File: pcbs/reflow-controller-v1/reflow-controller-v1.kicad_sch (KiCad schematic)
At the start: 19 parts, among them J1 PinHeader 1x03 P2.54mm, J101 EB163A-03-C-180, J102 EB163A-02-C-180, J103 EB163A-02-C-180, J104 EB163A-02-C-180, J105 EB163A-02-C-180, J106 PinHeader 1x03 P2.54mm, M101 47053-1000

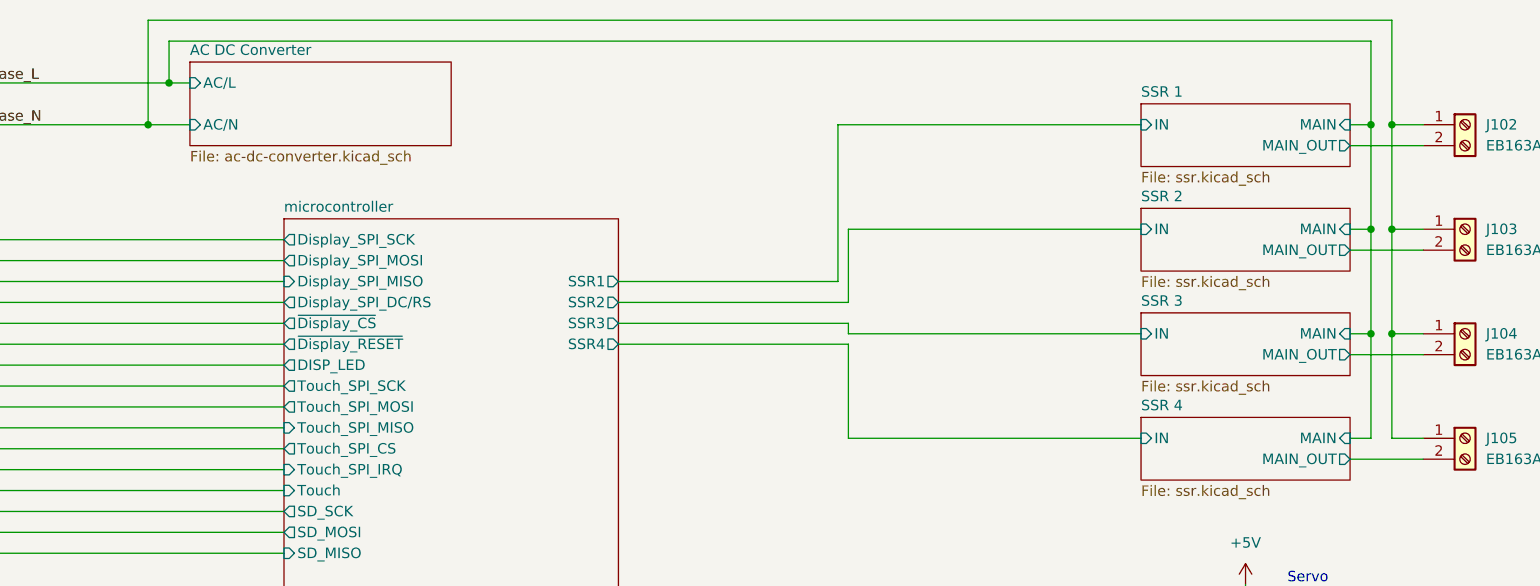
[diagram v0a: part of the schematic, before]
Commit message: add zero crossing detector
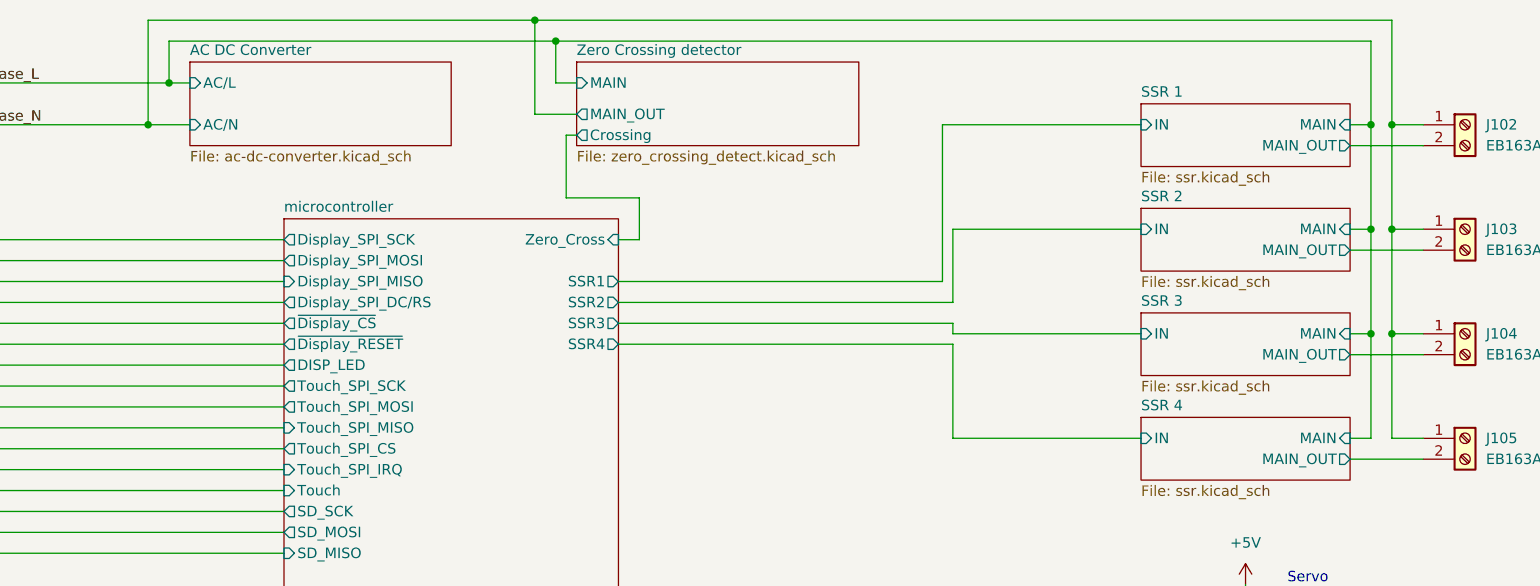
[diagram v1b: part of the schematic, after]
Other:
- added sheet Zero Crossing detector (zero_crossing_detect.kicad_sch)
- sheet microcontroller ports: added Zero_Cross; removed none
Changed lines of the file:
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@@
 	)
 	(junction
+		(at 132.08 13.97)
+		(diameter 0)
+		(color 0 0 0 0)
+	)
+	(junction
 		(at 233.68 39.37)
 		(diameter 0)
@@
 		(color 0 0 0 0)
 	)
+	(junction
+		(at 134.62 16.51)
+		(diameter 0)
+		(color 0 0 0 0)
+	)
 	(no_connect
 		(at 240.03 139.7)
@@
 	(wire
 		(pts
+			(xy 134.62 16.51) (xy 233.68 16.51)
+		)
+		(stroke
+			(width 0)
+			(type default)
+		)
+	)
+	(wire
+		(pts
 			(xy 133.35 167.64) (xy 133.35 177.8)
 		)
@@
 	(wire
 		(pts
+			(xy 144.78 40.64) (xy 142.24 40.64)
+		)
+		(stroke
+			(width 0)
+			(type default)
+		)
+	)
+	(wire
+		(pts
 			(xy 185.42 121.92) (xy 185.42 132.08)
 		)
@@
 	(wire
 		(pts
-			(xy 142.24 50.8) (xy 170.18 50.8)
+			(xy 142.24 50.8) (xy 182.88 50.8)
 		)
 		(stroke
@@
 	(wire
 		(pts
-			(xy 170.18 52.07) (xy 205.74 52.07)
+			(xy 182.88 52.07) (xy 205.74 52.07)
 		)
 		(stroke
@@
 	(wire
 		(pts
-			(xy 205.74 64.77) (xy 170.18 64.77)
+			(xy 205.74 64.77) (xy 182.88 64.77)
 		)
 		(stroke
@@
 	(wire
 		(pts
+			(xy 137.16 21.59) (xy 134.62 21.59)
+		)
+		(stroke
+			(width 0)
+			(type default)
+		)
+	)
+	(wire
+		(pts
 			(xy 54.61 144.78) (xy 101.6 144.78)
 		)
@@
 	(wire
 		(pts
-			(xy 168.91 45.72) (xy 168.91 26.67)
+			(xy 181.61 45.72) (xy 181.61 26.67)
 		)
 		(stroke
@@
 	(wire
 		(pts
-			(xy 142.24 48.26) (xy 170.18 48.26)
+			(xy 142.24 48.26) (xy 182.88 48.26)
+		)
+		(stroke
+			(width 0)
+			(type default)
+		)
+	)
+	(wire
+		(pts
+			(xy 135.89 35.56) (xy 144.78 35.56)
 		)
 		(stroke
@@
 	(wire
 		(pts
+			(xy 137.16 25.4) (xy 132.08 25.4)
+		)
+		(stroke
+			(width 0)
+			(type default)
+		)
+	)
+	(wire
+		(pts
 			(xy 49.53 63.5) (xy 101.6 63.5)
 		)
@@
 	(wire
 		(pts
+			(xy 137.16 27.94) (xy 135.89 27.94)
+		)
+		(stroke
+			(width 0)
+			(type default)
+		)
+	)
+	(wire
+		(pts
 			(xy 49.53 71.12) (xy 101.6 71.12)
 		)
@@
 	(wire
 		(pts
-			(xy 236.22 13.97) (xy 85.09 13.97)
+			(xy 144.78 35.56) (xy 144.78 40.64)
+		)
+		(stroke
+			(width 0)
+			(type default)
+		)
+	)
+	(wire
+		(pts
+			(xy 236.22 13.97) (xy 132.08 13.97)
 		)
 		(stroke
@@
 	(wire
 		(pts
-			(xy 170.18 50.8) (xy 170.18 52.07)
+			(xy 182.88 50.8) (xy 182.88 52.07)
 		)
 		(stroke
@@
 	(wire
 		(pts
-			(xy 168.91 26.67) (xy 205.74 26.67)
+			(xy 181.61 26.67) (xy 205.74 26.67)
 		)
 		(stroke
@@
 	(wire
 		(pts
-			(xy 142.24 45.72) (xy 168.91 45.72)
+			(xy 87.63 16.51) (xy 134.62 16.51)
+		)
+		(stroke
+			(width 0)
+			(type default)
+		)
+	)
+	(wire
+		(pts
+			(xy 142.24 45.72) (xy 181.61 45.72)
 		)
 		(stroke
@@
 	(wire
 		(pts
-			(xy 87.63 16.51) (xy 233.68 16.51)
+			(xy 231.14 29.21) (xy 240.03 29.21)
 		)
 		(stroke
@@
 	(wire
 		(pts
-			(xy 231.14 29.21) (xy 240.03 29.21)
+			(xy 54.61 144.78) (xy 54.61 165.1)
 		)
 		(stroke
@@
 	(wire
 		(pts
-			(xy 54.61 144.78) (xy 54.61 165.1)
+			(xy 72.39 162.56) (xy 49.53 162.56)
 		)
 		(stroke
@@
 	(wire
 		(pts
-			(xy 72.39 162.56) (xy 49.53 162.56)
+			(xy 71.12 138.43) (xy 101.6 138.43)
 		)
 		(stroke
@@
 	(wire
 		(pts
-			(xy 71.12 138.43) (xy 101.6 138.43)
+			(xy 99.06 149.86) (xy 99.06 152.4)
 		)
 		(stroke
@@
 	(wire
 		(pts
-			(xy 99.06 149.86) (xy 99.06 152.4)
+			(xy 134.62 21.59) (xy 134.62 16.51)
 		)
 		(stroke
@@
 	(wire
 		(pts
-			(xy 170.18 64.77) (xy 170.18 53.34)
+			(xy 182.88 64.77) (xy 182.88 53.34)
 		)
 		(stroke
@@
 	(wire
 		(pts
-			(xy 170.18 53.34) (xy 142.24 53.34)
+			(xy 182.88 53.34) (xy 142.24 53.34)
 		)
 		(stroke
@@
 	(wire
 		(pts
+			(xy 132.08 13.97) (xy 85.09 13.97)
+		)
+		(stroke
+			(width 0)
+			(type default)
+		)
+	)
+	(wire
+		(pts
 			(xy 49.53 76.2) (xy 101.6 76.2)
 		)
@@
 	(wire
 		(pts
-			(xy 170.18 48.26) (xy 170.18 39.37)
+			(xy 182.88 48.26) (xy 182.88 39.37)
 		)
 		(stroke
@@
 	(wire
 		(pts
+			(xy 135.89 27.94) (xy 135.89 35.56)
+		)
+		(stroke
+			(width 0)
+			(type default)
+		)
+	)
+	(wire
+		(pts
 			(xy 49.53 50.8) (xy 101.6 50.8)
 		)
@@
 	(wire
 		(pts
+			(xy 132.08 25.4) (xy 132.08 13.97)
+		)
+		(stroke
+			(width 0)
+			(type default)
+		)
+	)
+	(wire
+		(pts
 			(xy 220.98 114.3) (xy 218.44 114.3)
 		)
@@
 	(wire
 		(pts
-			(xy 170.18 39.37) (xy 205.74 39.37)
+			(xy 182.88 39.37) (xy 205.74 39.37)
 		)
 		(stroke
@@
 	)
 	(sheet
+		(at 137.16 19.05)
+		(size 34.29 10.16)
+		(fields_autoplaced yes)
+		(stroke
+			(width 0.1524)
+			(type solid)
+		)
+		(fill
+			(color 0 0 0 0.0000)
+		)
+		(property "Sheetname" "Zero Crossing detector"
+			(at 137.16 18.3384 0)
+			(effects
+				(font
+					(size 1.27 1.27)
+				)
+				(justify left bottom)
+			)
+		)
+		(property "Sheetfile" "zero_crossing_detect.kicad_sch"
+			(at 137.16 29.7946 0)
+			(effects
+				(font
+					(size 1.27 1.27)
+				)
+				(justify left top)
+			)
+		)
+		(property "Field2" ""
+			(at 137.16 19.05 0)
+			(effects
+				(font
+					(size 1.27 1.27)
+				)
+				(hide yes)
+			)
+		)
+		(pin "MAIN" input
+			(at 137.16 21.59 180)
+			(effects
+				(font
+					(size 1.27 1.27)
+				)
+				(justify left)
+			)
+		)
+		(pin "MAIN_OUT" output
+			(at 137.16 25.4 180)
+			(effects
+				(font
+					(size 1.27 1.27)
+				)
+				(justify left)
+			)
+		)
+		(pin "Crossing" output
+			(at 137.16 27.94 180)
+			(effects
+				(font
+					(size 1.27 1.27)
+				)
+				(justify left)
+			)
+		)
+		(instances
+			(project "reflow-controller-v1"
+				(path "/843848ae-bf49-42cb-8f8b-76790d2e568d"
+					(page "16")
+				)
+			)
+		)
+	)
+	(sheet
 		(at 101.6 38.1)
 		(size 40.64 129.54)
@@
 			)
 		)
+		(pin "Zero_Cross" input
+			(at 142.24 40.64 0)
+			(effects
+				(font
+					(size 1.27 1.27)
+				)
+				(justify right)
+			)
+		)

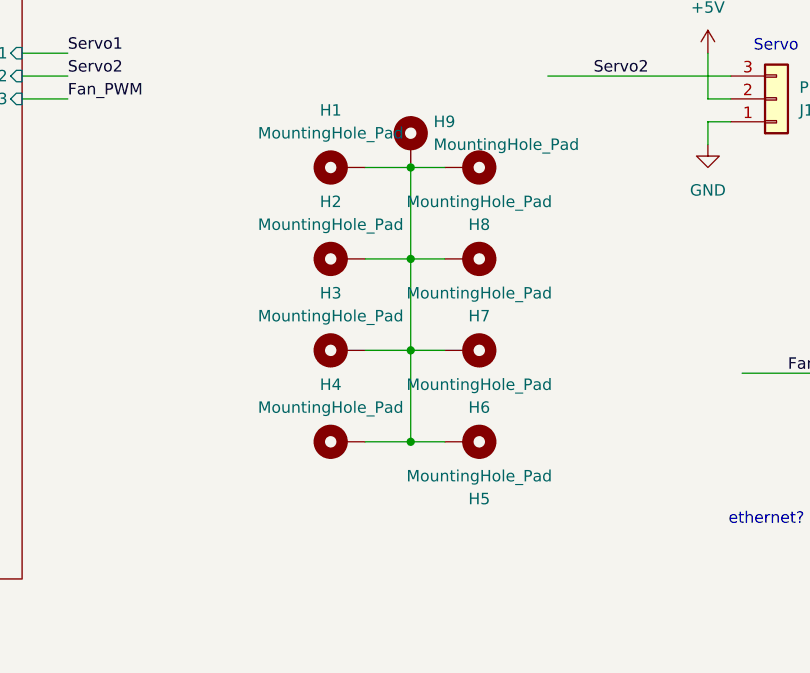
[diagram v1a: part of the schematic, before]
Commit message: update display placing & prelim. routing
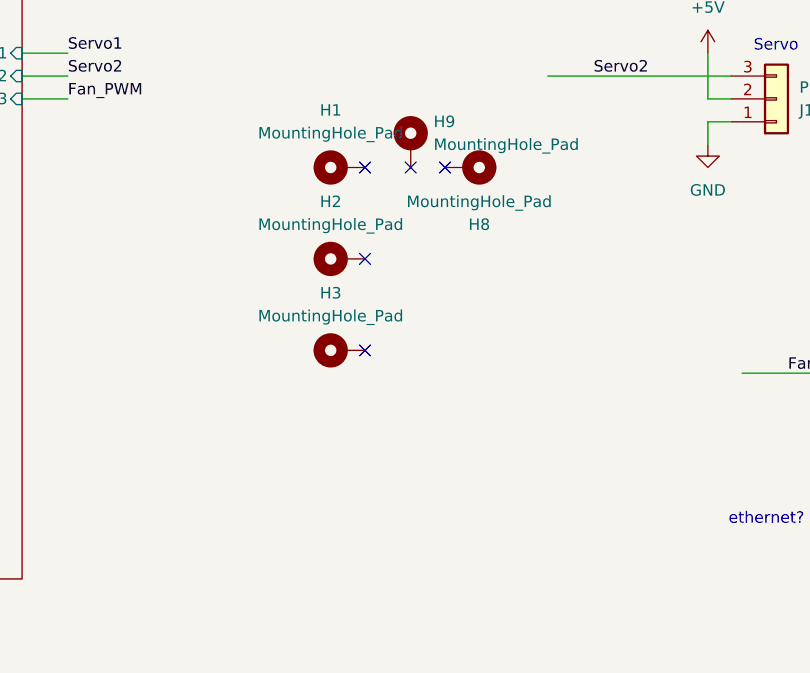
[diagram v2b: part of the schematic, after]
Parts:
- removed H4, H5, H6, H7: MountingHole_Pad, Mounting_Wuerth:Mounting_Wuerth_WA-SMSI-M3_H15mm_9774150360, symbol Mechanical:MountingHole_Pad
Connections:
- now unconnected: H1.1, H2.1, H3.1, H8.1, H9.1
- no-connect marks 1 -> 6
